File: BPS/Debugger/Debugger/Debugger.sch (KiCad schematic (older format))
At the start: 22 parts, among them J1 Conn_01x03, SW1 Switch:SW_Push, U1 STM32F413RHTx, Y1 Crystal

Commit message: commit
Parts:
- SW1: symbol BPSMaster-cache:Switch:SW_Push -> Debugger-rescue:Switch_SW_Push-BPSMaster-cache
- U1: symbol BPSMaster-cache:STM32F413RHTx -> Debugger-rescue:STM32F413RHTx-BPSMaster-cache
- U2: renamed from U?; symbol BPSMaster-cache:NCP1117-3.3_SOT223 -> Debugger-rescue:NCP1117-3.3_SOT223-BPSMaster-cache
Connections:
- net labels added: +5V
- wire segments 94 -> 102
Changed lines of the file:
@@
 EESchema Schematic File Version 4
+LIBS:Debugger-cache
 EELAYER 26 0
 EELAYER END
 $Descr A4 11693 8268
 encoding utf-8
-Sheet 1 1
+Sheet 1 2
 Title ""
 Date ""
@@
 $EndDescr
 $Comp
-L BPSMaster-cache:+3.3V #PWR04
+L Debugger-rescue:+3.3V-BPSMaster-cache #PWR04
 U 1 1 5C5F34E7
 P 5050 2300
@@
 Connection ~ 4250 3000
 $Comp
-L BPSMaster-cache:STM32F413RHTx U1
+L Debugger-rescue:STM32F413RHTx-BPSMaster-cache U1
 U 1 1 5C5F31C3
 P 5250 4100
@@
 $EndComp
 $Comp
-L BPSMaster-cache:+3.3V #PWR06
+L Debugger-rescue:+3.3V-BPSMaster-cache #PWR06
 U 1 1 5C5FD9D5
 P 6150 1150
@@
 $EndComp
 $Comp
-L BPSMaster-cache:+3.3V #PWR08
+L Debugger-rescue:+3.3V-BPSMaster-cache #PWR08
 U 1 1 5C60EE5B
 P 6650 2500
@@
 	6650 2550 6650 2600
 $Comp
-L BPSMaster-cache:Switch:SW_Push SW1
+L Debugger-rescue:Switch_SW_Push-BPSMaster-cache SW1
 U 1 1 5C616023
 P 8300 2750
@@
 	4000 3800 4550 3800
 $Comp
-L power:GND #PWR?
+L power:GND #PWR016
 U 1 1 5C62A6C5
 P 3550 1750
-F 0 "#PWR?" H 3550 1500 50  0001 C CNN
+F 0 "#PWR016" H 3550 1500 50  0001 C CNN
 F 1 "GND" H 3555 1577 50  0000 C CNN
 F 2 "" H 3550 1750 50  0001 C CNN
@@
 $EndComp
 $Comp
-L power:+12V #PWR?
+L power:+12V #PWR015
 U 1 1 5C62A736
 P 3150 1200
-F 0 "#PWR?" H 3150 1050 50  0001 C CNN
+F 0 "#PWR015" H 3150 1050 50  0001 C CNN
 F 1 "+12V" H 3165 1373 50  0000 C CNN
 F 2 "" H 3150 1200 50  0001 C CNN
@@
 	6150 1800 6150 1900
 $Comp
-L BPSMaster-cache:NCP1117-3.3_SOT223 U?
+L Debugger-rescue:NCP1117-3.3_SOT223-BPSMaster-cache U2
 U 1 1 5C65BF96
 P 3550 1350
-F 0 "U?" H 3550 1592 50  0000 C CNN
+F 0 "U2" H 3550 1592 50  0000 C CNN
 F 1 "NCP1117-3.3_SOT223" H 3550 1501 50  0000 C CNN
 F 2 "Package_TO_SOT_SMD:SOT-223-3_TabPin2" H 3550 1550 50  0001 C CNN
@@
 Text Label 6350 5200 2    50   ~ 0
 CAN1_TX
+$Sheet
+S 1050 1650 1750 1000
+U 5C5F7A4D
+F0 "Sheet5C5F7A4C" 50
+F1 "file5C5F7A4C.sch" 50
+F2 "+5V" I R 2800 1850 50
+F3 "GND" I R 2800 2450 50
+F4 "CAN_TX" I R 2800 2150 50
+F5 "CAN_RX" I R 2800 2300 50
+F6 "+3.3V" I R 2800 2000 50
+$EndSheet
+Wire Wire Line
+	2800 1850 2950 1850
+Wire Wire Line
+	2950 1850 2950 1750
+Wire Wire Line
+	3100 2000 3100 1900
+Wire Wire Line
+	2800 2000 3100 2000
+Wire Wire Line
+	2800 2150 3200 2150
+Wire Wire Line
+	2800 2300 3200 2300
+Wire Wire Line
+	2800 2450 3000 2450
+Wire Wire Line
+	3000 2450 3000 2550
+$Comp
+L power:GND #PWR013
+U 1 1 5C62A244
+P 3000 2550
+F 0 "#PWR013" H 3000 2300 50  0001 C CNN
+F 1 "GND" H 3005 2377 50  0000 C CNN
+F 2 "" H 3000 2550 50  0001 C CNN
+F 3 "" H 3000 2550 50  0001 C CNN
+	1    3000 2550
+	1    0    0    -1
+$EndComp
+$Comp
+L power:+5V #PWR012
+U 1 1 5C62A371
+P 2950 1750
+F 0 "#PWR012" H 2950 1600 50  0001 C CNN
+F 1 "+5V" H 2965 1923 50  0000 C CNN
+F 2 "" H 2950 1750 50  0001 C CNN
+F 3 "" H 2950 1750 50  0001 C CNN
+	1    2950 1750
+	1    0    0    -1
+$EndComp
+$Comp
+L power:+3.3V #PWR014
+U 1 1 5C62A3DB
+P 3100 1900
+F 0 "#PWR014" H 3100 1750 50  0001 C CNN
+F 1 "+3.3V" H 3115 2073 50  0000 C CNN
+F 2 "" H 3100 1900 50  0001 C CNN
+F 3 "" H 3100 1900 50  0001 C CNN
+	1    3100 1900
+	1    0    0    -1
+$EndComp
+Text Label 2950 2150 0    50   ~ 0
+CAN1_TX
+Text Label 2950 2300 0    50   ~ 0
+CAN1_RX
 $EndSCHEMATC

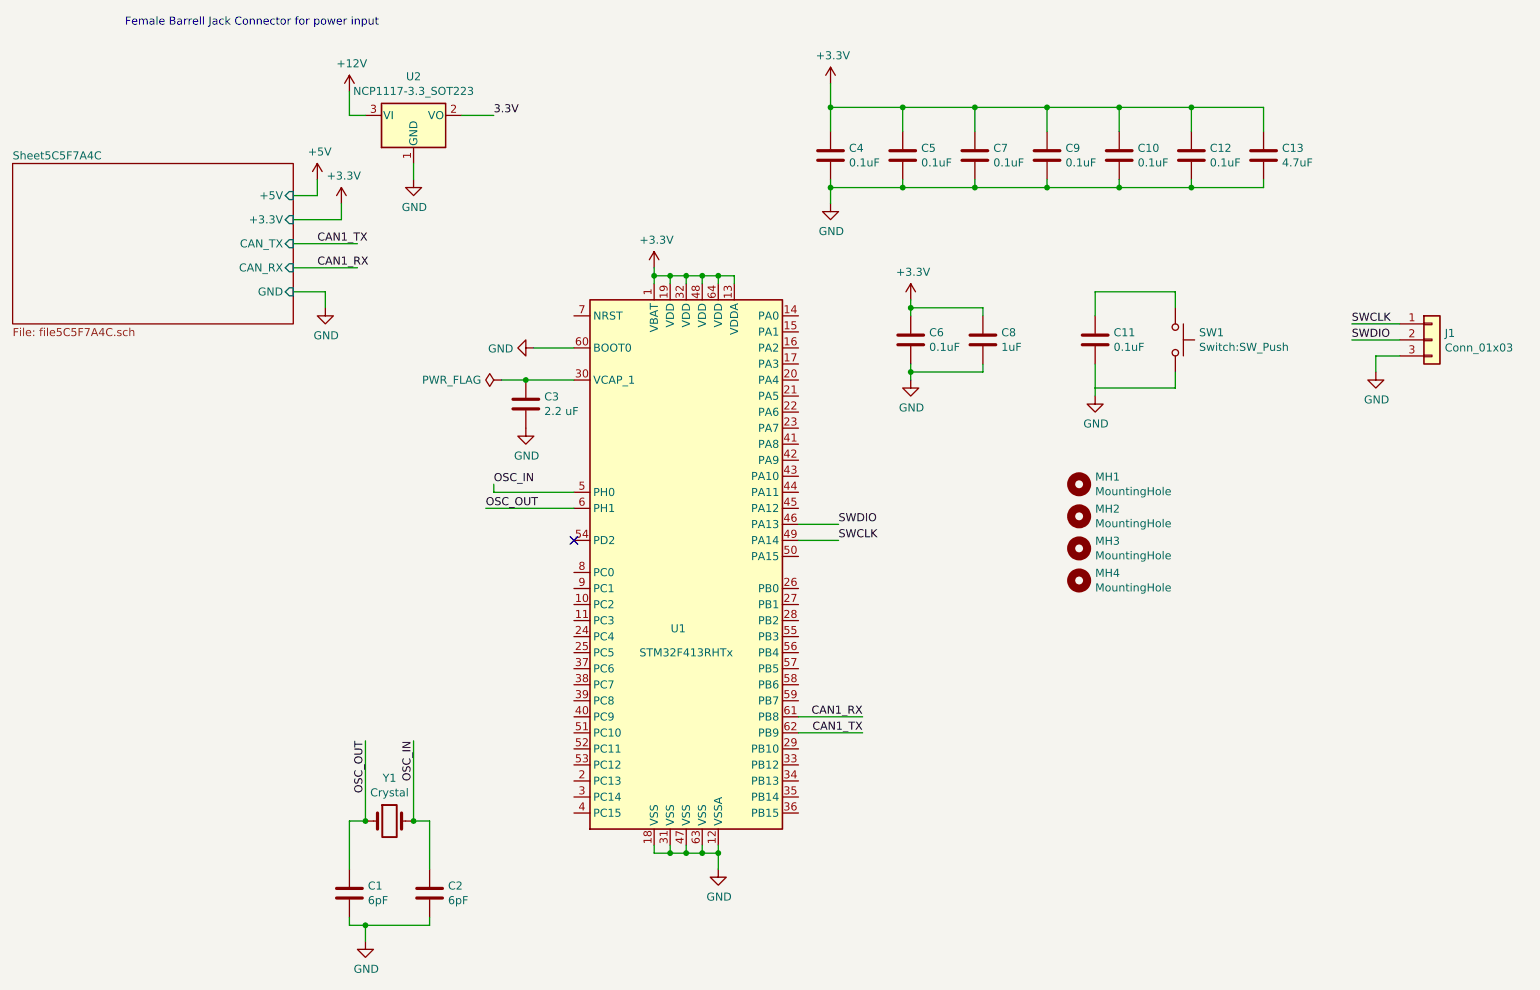
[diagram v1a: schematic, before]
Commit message: NC flags, 3.3v flag, etc.
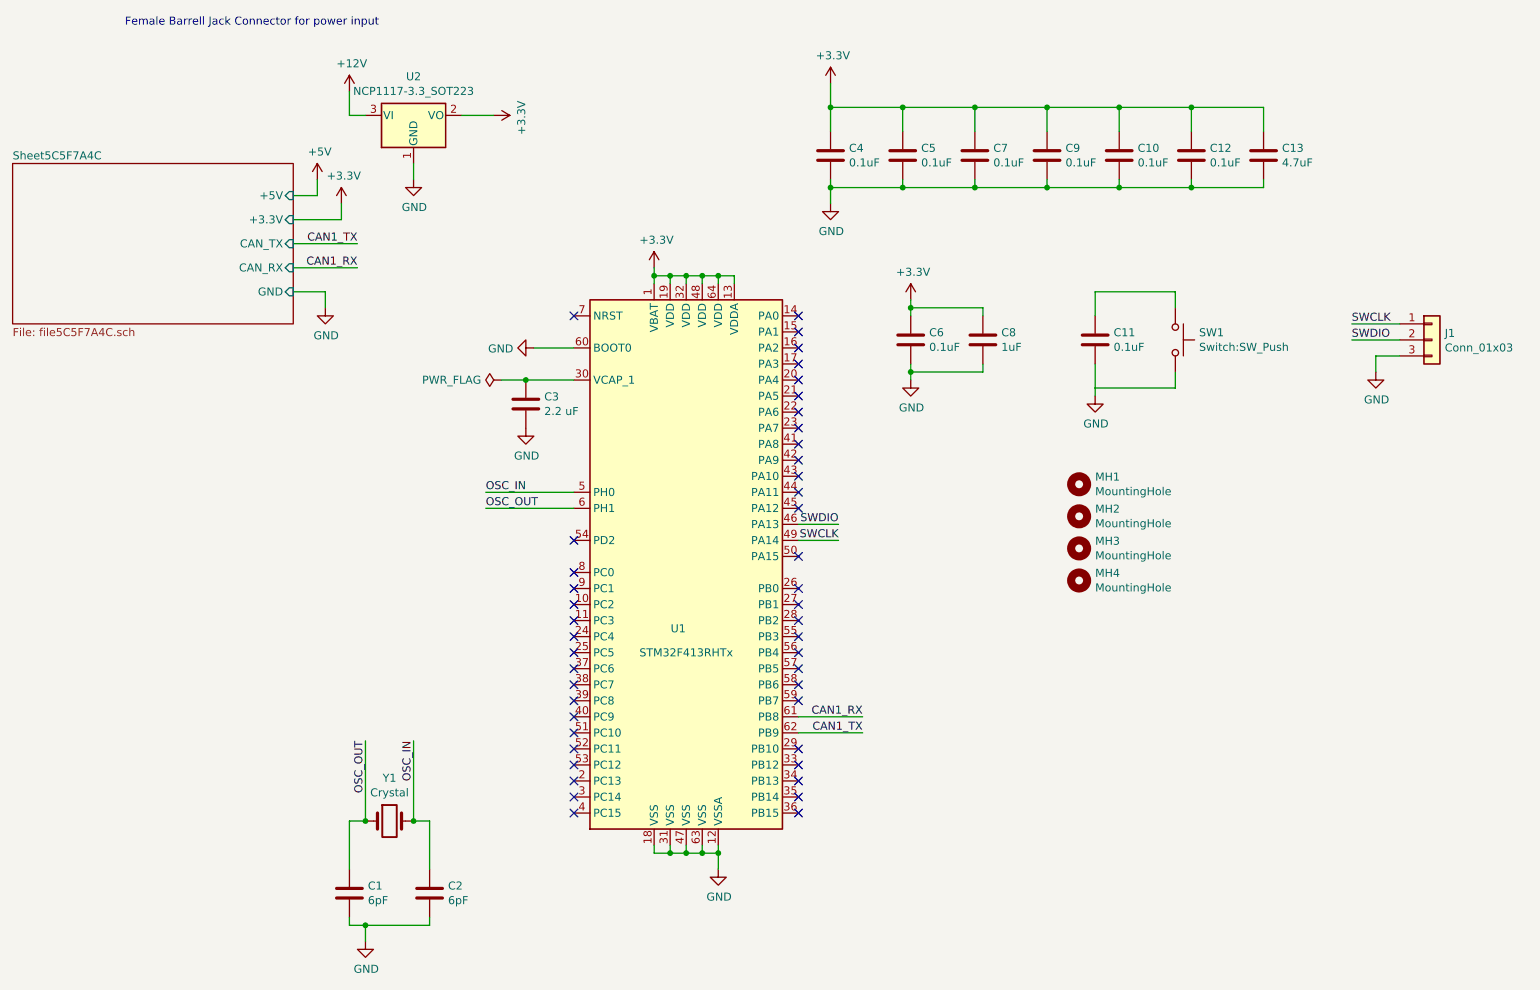
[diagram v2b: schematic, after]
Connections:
- net 3.3V is gone; now on net +3V3: U2.2 (VO)
- no-connect marks 1 -> 45
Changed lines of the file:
@@
 	1    0    0    -1
 $EndComp
-Text Label 4050 3650 0    50   ~ 0
+Text Label 4000 3700 0    50   ~ 0
 OSC_IN
 Text Label 4000 3800 0    50   ~ 0
@@
 Wire Wire Line
 	7800 3050 7800 3100
-Text Label 6200 3900 0    50   ~ 0
+Text Label 6200 3900 2    50   ~ 0
 SWDIO
-Text Label 6200 4000 0    50   ~ 0
+Text Label 6200 4000 2    50   ~ 0
 SWCLK
 Wire Wire Line
@@
 	9550 2850 9700 2850
 Wire Wire Line
-	4050 3700 4050 3650
-Wire Wire Line
-	4050 3700 4550 3700
-Wire Wire Line
 	4000 3800 4550 3800
 $Comp
@@
 	1    0    0    -1
 $EndComp
-Text Label 4050 1350 0    50   ~ 0
-3.3V
 Wire Wire Line
 	3150 1200 3150 1350
 Wire Wire Line
 	3150 1350 3250 1350
-Wire Wire Line
-	3850 1350 4050 1350
 Wire Wire Line
 	3550 1650 3550 1750
@@
 	1    0    0    -1
 $EndComp
-Text Label 2950 2150 0    50   ~ 0
+Text Label 3200 2150 2    50   ~ 0
 CAN1_TX
-Text Label 2950 2300 0    50   ~ 0
+Text Label 3200 2300 2    50   ~ 0
 CAN1_RX
+$Comp
+L Debugger-rescue:+3.3V-BPSMaster-cache #PWR020
+U 1 1 5C68CA74
+P 4050 1350
+F 0 "#PWR020" H 4050 1200 50  0001 C CNN
+F 1 "+3.3V" H 4065 1523 50  0000 C CNN
+F 2 "" H 4050 1350 50  0001 C CNN
+F 3 "" H 4050 1350 50  0001 C CNN
+	1    4050 1350
+	0    1    1    0
+$EndComp
+Wire Wire Line
+	3850 1350 4050 1350
+Wire Wire Line
+	4000 3700 4550 3700
+NoConn ~ 5950 2600
+NoConn ~ 5950 2700
+NoConn ~ 5950 2800
+NoConn ~ 5950 2900
+NoConn ~ 5950 3000
+NoConn ~ 5950 3100
+NoConn ~ 5950 3200
+NoConn ~ 5950 3300
+NoConn ~ 5950 3400
+NoConn ~ 5950 3500
+NoConn ~ 5950 3600
+NoConn ~ 5950 3700
+NoConn ~ 5950 3800
+NoConn ~ 5950 4100
+NoConn ~ 5950 4300
+NoConn ~ 5950 4400
+NoConn ~ 5950 4500
+NoConn ~ 5950 4600
+NoConn ~ 5950 4700
+NoConn ~ 5950 4800
+NoConn ~ 5950 4900
+NoConn ~ 5950 5000
+NoConn ~ 5950 5300
+NoConn ~ 5950 5400
+NoConn ~ 5950 5500
+NoConn ~ 5950 5600
+NoConn ~ 5950 5700
+NoConn ~ 4550 5700
+NoConn ~ 4550 5600
+NoConn ~ 4550 5500
+NoConn ~ 4550 5400
+NoConn ~ 4550 5300
+NoConn ~ 4550 5200
+NoConn ~ 4550 5100
+NoConn ~ 4550 5000
+NoConn ~ 4550 4900
+NoConn ~ 4550 4800
+NoConn ~ 4550 4700
+NoConn ~ 4550 4600
+NoConn ~ 4550 4500
+NoConn ~ 4550 4400
+NoConn ~ 4550 4300
+NoConn ~ 4550 4200
+NoConn ~ 4550 2600
 $EndSCHEMATC

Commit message: debugger
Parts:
- added D2, D3, D4: LED, LED_SMD:LED_0805_2012Metric, symbol Device:LED
- added R5, R6, R7: 750, Resistor_SMD:R_0805_2012Metric, symbol Device:R
- C1, C10, C11, C12, C13, C2, C3, C4, C5, C6, C7, C8, C9: footprint (none) -> Capacitor_SMD:C_0805_2012Metric
- J1: footprint (none) -> Connector_PinHeader_2.54mm:PinHeader_1x02_P2.54mm_Vertical
- MH1, MH2, MH3, MH4: footprint (none) -> MountingHole:MountingHole_3mm
- SW1: footprint (none) -> Button_Switch_SMD:SW_SPST_B3SL-1002P
- Y1: footprint (none) -> UTSVT_BPS:NX8045GB-8.000M-STD-CSJ-1
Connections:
- net GND: now also R5.2, R6.2, R7.2
- net PC8: now reaches U1.39 (PC8)
- net PC8: now also D2.2 (A)
- net PC9: now reaches U1.40 (PC9)
- net PC9: now also D3.2 (A)
- net PC10: now reaches U1.51 (PC10)
- net PC10: now also D4.2 (A)
- net NRST: now reaches U1.7 (NRST)
- net NRST: now also C11.1, SW1.1
- new net: D2.1 (K), R5.1
- new net: D3.1 (K), R6.1
- new net: D4.1 (K), R7.1
- no-connect marks 45 -> 41
